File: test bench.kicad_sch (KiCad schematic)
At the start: 0 parts

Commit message: Added components
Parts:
- added A1: Arduino_UNO_R3, Module:Arduino_UNO_R3, symbol MCU_Module:Arduino_UNO_R3
- added RV1, RV2, RV3: R_Potentiometer, symbol Device:R_Potentiometer
- added SW1, SW2: SW_SP3T, symbol Switch:SW_SP3T
- added SW3: SW_Push, symbol Switch:SW_Push

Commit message: Added components
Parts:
- added RV4, RV5: R_Potentiometer, symbol Device:R_Potentiometer
- added SW4: SW_DPST_x2, symbol Switch:SW_DPST_x2

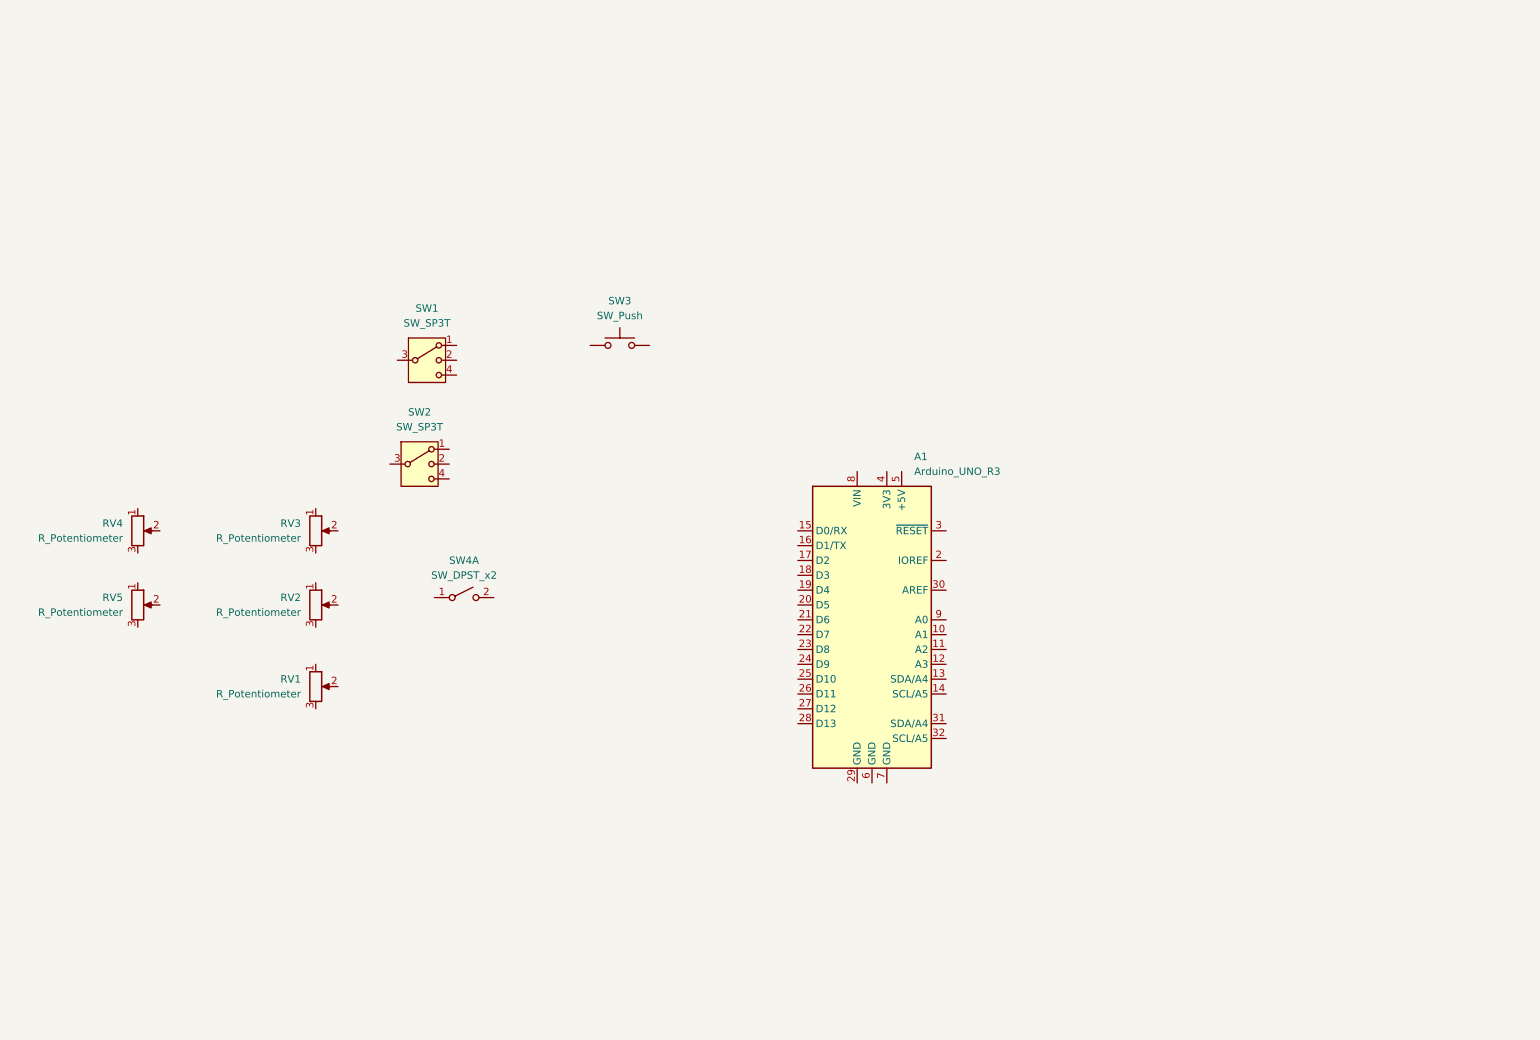
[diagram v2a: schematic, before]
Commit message: added components
Added additional components
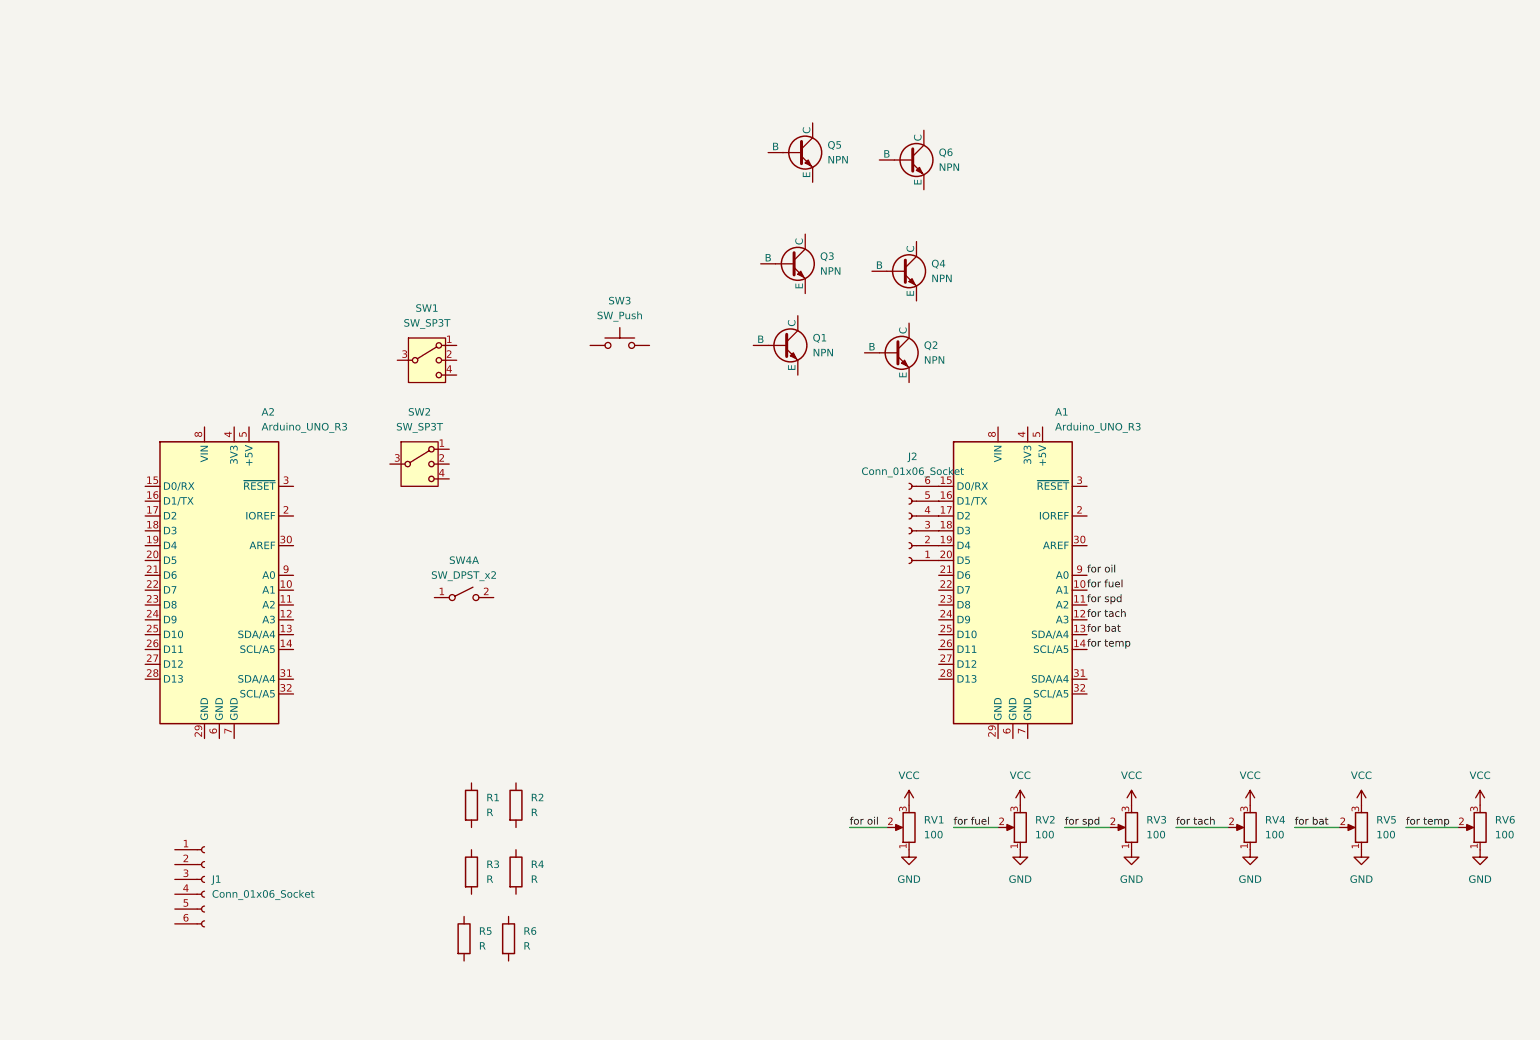
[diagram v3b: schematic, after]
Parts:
- added A2: Arduino_UNO_R3, Module:Arduino_UNO_R3, symbol MCU_Module:Arduino_UNO_R3
- added J1, J2: Conn_01x06_Socket, symbol Connector:Conn_01x06_Socket
- added Q1, Q2, Q3, Q4, Q5, Q6: NPN, symbol Simulation_SPICE:NPN
- added R1, R2, R3, R4, R5, R6: R, symbol Device:R
- added RV6: 100, symbol Device:R_Potentiometer
- RV1, RV2, RV3, RV4, RV5: value R_Potentiometer -> 100
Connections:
- net for fuel: now reaches A1.10 (A1)
- net for fuel: now also RV2.2
- net for spd: now reaches A1.11 (A2)
- net for spd: now also RV3.2
- net for tach: now reaches A1.12 (A3)
- net for tach: now also RV4.2
- net for bat: now reaches A1.13 (SDA/A4)
- net for bat: now also RV5.2
- net for temp: now reaches A1.14 (SCL/A5)
- net for temp: now also RV6.2
- net at A1.15 (D0/RX): now also J2.6 (Pin_6)
- net at A1.16 (D1/TX): now also J2.5 (Pin_5)
- net at A1.17 (D2): now also J2.4 (Pin_4)
- net at A1.18 (D3): now also J2.3 (Pin_3)
- net at A1.19 (D4): now also J2.2 (Pin_2)
- net at A1.20 (D5): now also J2.1 (Pin_1)
- net for oil: now reaches A1.9 (A0)
- net for oil: now also RV1.2
- net GND: now reaches RV2.1
- net GND: now also RV1.1, RV3.1, RV4.1, RV5.1, RV6.1
- net VCC: now reaches RV2.3
- net VCC: now also RV1.3, RV3.3, RV4.3, RV5.3, RV6.3
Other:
- moved on the sheet: A1, RV1, RV2, RV3, RV4, RV5

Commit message: Update test bench.kicad_sch
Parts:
- added R10, R11, R12, R7, R8, R9: R, symbol Device:R
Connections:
- net GND: now also A1.29 (GND), A1.6 (GND), A1.7 (GND), A2.29 (GND), A2.6 (GND), A2.7 (GND), R1.2, R2.2, R3.2, R4.2, R5.2, R6.2, R10.2, R11.2, R12.2, R7.2, R8.2, R9.2; no longer RV1.1, RV2.1, RV3.1, RV4.1, RV5.1, RV6.1
- net VCC: now also A1.8 (VIN), A2.8 (VIN), SW1.3, SW2.3, SW3.1, SW4.1 (A)
- net HG Beam: now reaches R4.1
- net HG Beam: now also A2.12 (A3), J1.3 (Pin_3), SW1.1
- net LW Beam: now reaches R3.1
- net LW Beam: now also A2.11 (A2), J1.4 (Pin_4), SW1.4
- net BK Switch: now reaches SW3.2
- net BK Switch: now also A2.13 (SDA/A4), J1.2 (Pin_2), R5.1
- net LF Turn: now reaches SW2.1
- net LF Turn: now also A2.10 (A1), J1.5 (Pin_5), R1.1
- net RT Turn: now reaches SW2.4
- net RT Turn: now also A2.9 (A0), J1.6 (Pin_6), R2.1
- net HAZRD: now reaches J1.1 (Pin_1)
- net HAZRD: now also A2.14 (SCL/A5), R6.1, SW4.2 (B)
- new net: R12.1, RV6.1
- new net: R7.1, RV1.1
- new net: R9.1, RV3.1
- new net: R8.1, RV2.1
- new net: R10.1, RV4.1
- new net: R11.1, RV5.1
- no-connect marks 0 -> 2
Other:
- moved on the sheet: A1, J1, J2, Q1, Q2, Q3, Q4, Q5, Q6, R1, R2, R3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

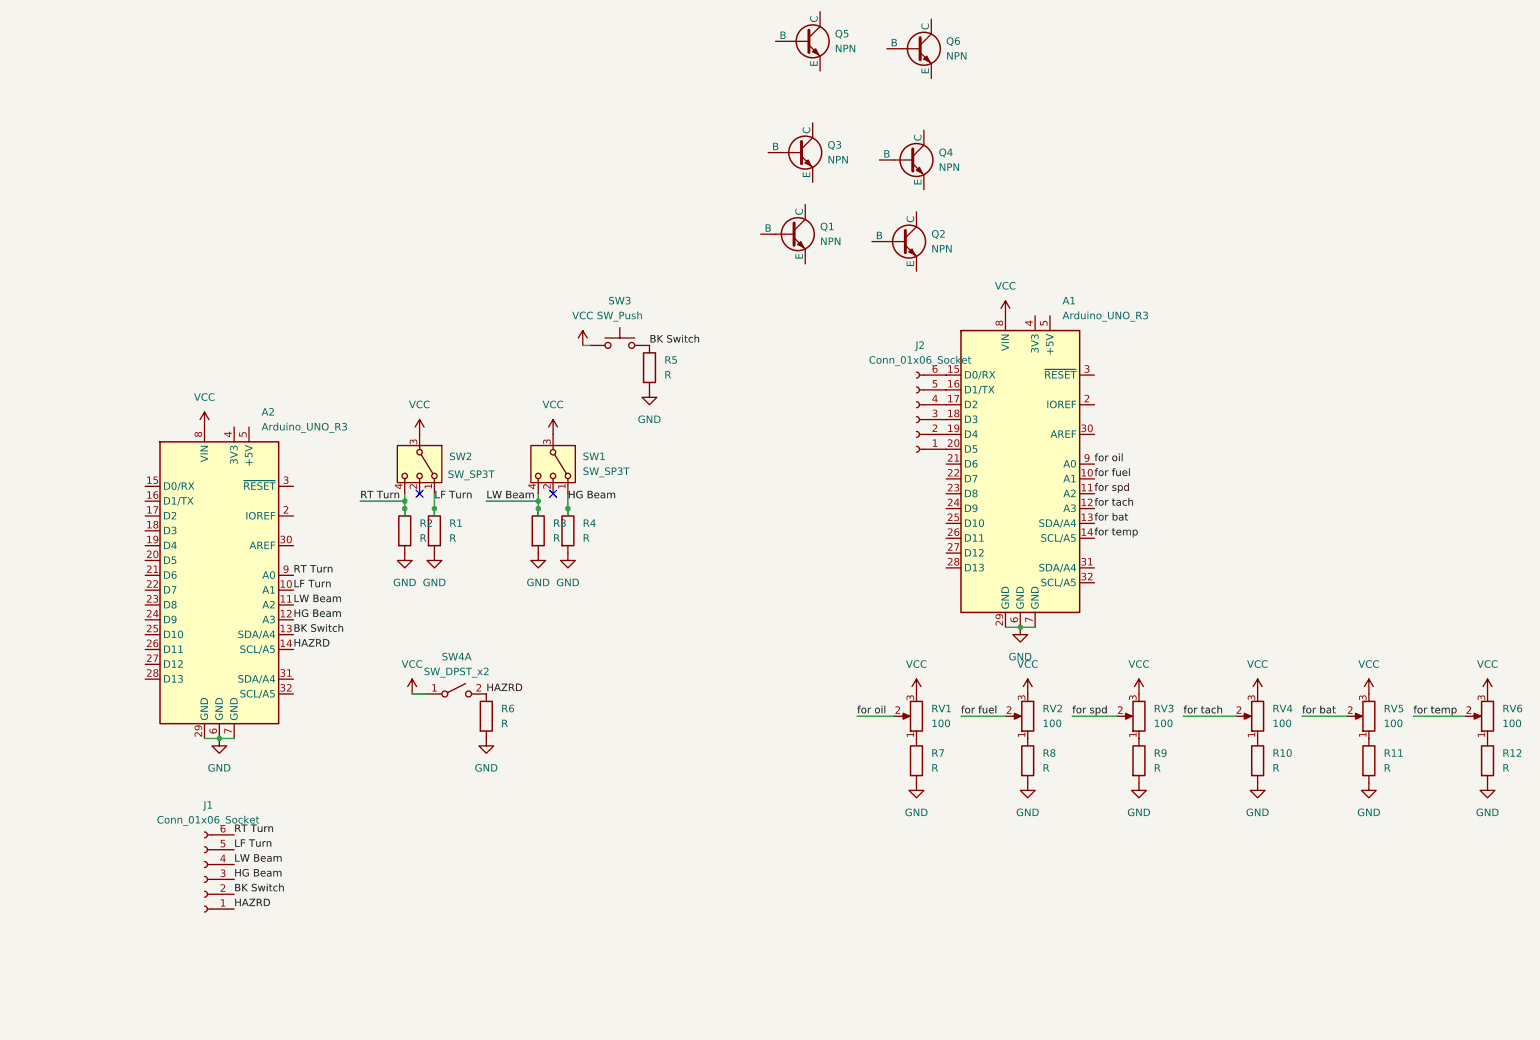
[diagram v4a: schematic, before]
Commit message: Update test bench.kicad_sch
changed arduinos to esp32
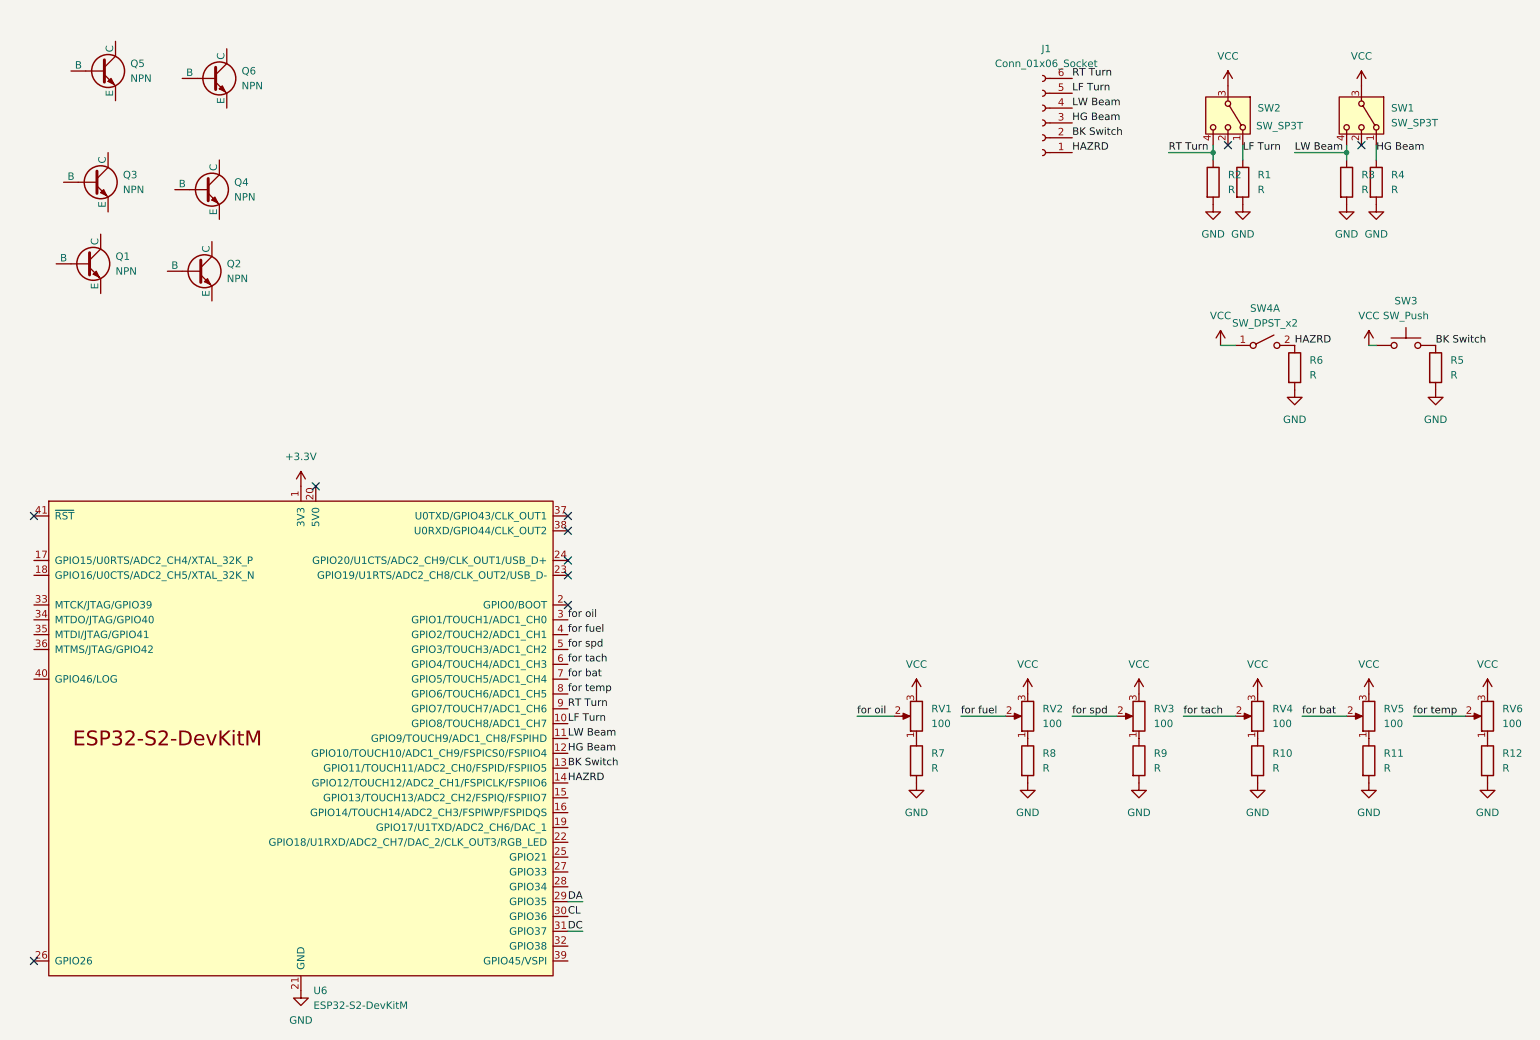
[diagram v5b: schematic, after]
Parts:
- removed A1, A2: Arduino_UNO_R3, Module:Arduino_UNO_R3, symbol MCU_Module:Arduino_UNO_R3
- removed J2: Conn_01x06_Socket, symbol Connector:Conn_01x06_Socket
- added U6: ESP32-S2-DevKitM, Espressif:ESP32-S2-DevKitM, symbol Espressif:ESP32-S2-DevKitM
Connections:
- net BK Switch: now also U6.13 (GPIO11/TOUCH11/ADC2_CH0/FSPID/FSPIIO5)
- net GND: now also U6.21 (GND), U6.42 (GND)
- net HAZRD: now also U6.14 (GPIO12/TOUCH12/ADC2_CH1/FSPICLK/FSPIIO6)
- net HG Beam: now also U6.12 (GPIO10/TOUCH10/ADC1_CH9/FSPICS0/FSPIIO4)
- net LF Turn: now also U6.10 (GPIO8/TOUCH8/ADC1_CH7)
- net LW Beam: now also U6.11 (GPIO9/TOUCH9/ADC1_CH8/FSPIHD)
- net RT Turn: now also U6.9 (GPIO7/TOUCH7/ADC1_CH6)
- net for bat: now also U6.7 (GPIO5/TOUCH5/ADC1_CH4)
- net for fuel: now also U6.4 (GPIO2/TOUCH2/ADC1_CH1)
- net for oil: now also U6.3 (GPIO1/TOUCH1/ADC1_CH0)
- net for spd: now also U6.5 (GPIO3/TOUCH3/ADC1_CH2)
- net for tach: now also U6.6 (GPIO4/TOUCH4/ADC1_CH3)
- net for temp: now also U6.8 (GPIO6/TOUCH6/ADC1_CH5)
- new net +3.3V: U6.1 (3V3)
- new net CL: U6.30 (GPIO36)
- new net DA: U6.29 (GPIO35)
- new net DC: U6.31 (GPIO37)
- no-connect marks 2 -> 10
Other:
- moved on the sheet: J1, Q1, Q2, Q3, Q4, Q5, Q6, R1, R2, R3, R4, R5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
